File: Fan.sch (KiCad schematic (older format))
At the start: 9 parts, among them Q2 MOSFET_N, Q3 MOSFET_N, Q4 MOSFET_N, U6 MCP4921-E/P, U7 LM324

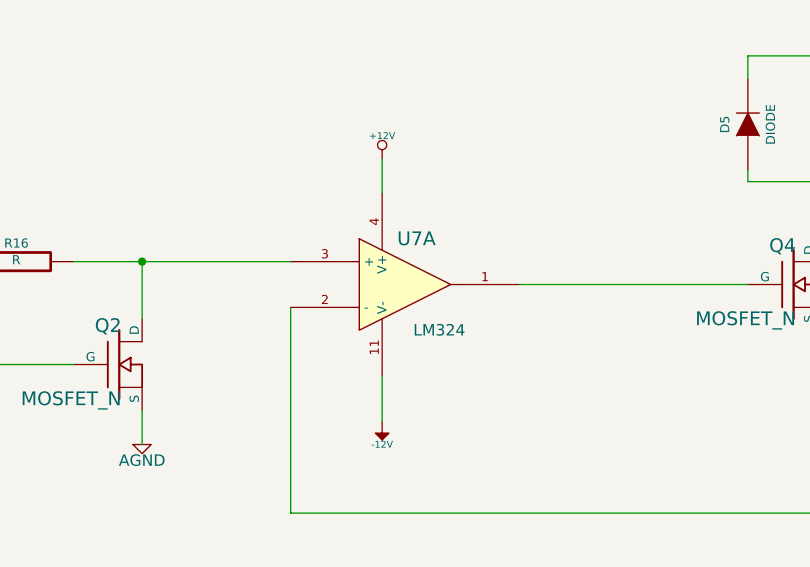
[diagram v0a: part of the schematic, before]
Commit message: Associated Thermocouple module
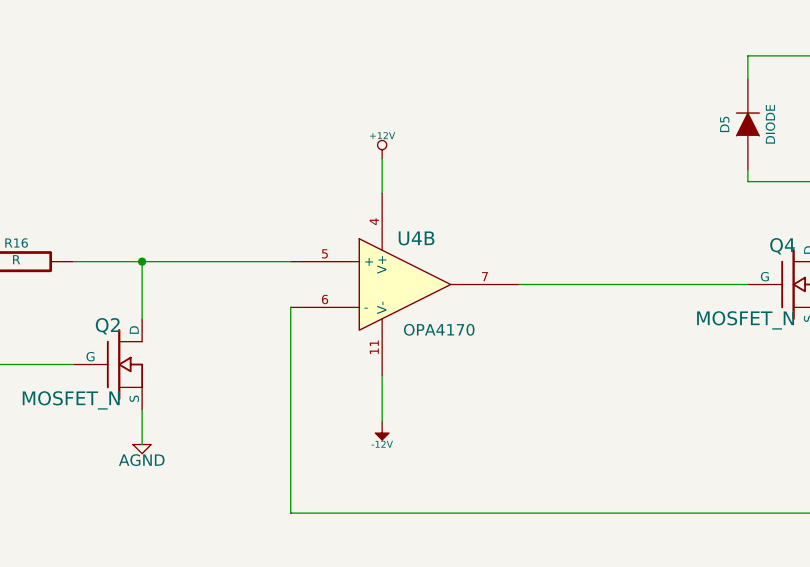
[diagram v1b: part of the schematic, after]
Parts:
- U4: renamed from U7; value LM324 -> OPA4170; MFG Part Number (none) -> OPA4170
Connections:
- net CURR_MEAS: now also U4.6 (-); no longer U4.2 (-)
- net at Q4.G: now also U4.7; no longer U4.1
- net at Q2.D, R16.2: now also U4.5 (+); no longer U4.3 (+)
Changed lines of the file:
@@
 FAN_PWM
 $Comp
-L LM324 U7
-U 1 1 52EF9EF8
+L LM324 U4
+U 2 1 52EF9EF8
 P 4400 2550
-F 0 "U7" H 4450 2750 60  0000 C CNN
-F 1 "LM324" H 4550 2350 50  0000 C CNN
+F 0 "U4" H 4450 2750 60  0000 C CNN
+F 1 "OPA4170" H 4550 2350 50  0000 C CNN
 F 2 "" H 4400 2550 60  0000 C CNN
 F 3 "" H 4400 2550 60  0000 C CNN
-	1    4400 2550
+F 4 "OPA4170" H 4400 2550 60  0001 C CNN "MFG Part Number"
+	2    4400 2550
 	1    0    0    -1
 $EndComp
@@
 $EndComp
 $Comp
-L AGND #PWR34
+L AGND #PWR035
 U 1 1 52EF9F60
 P 6200 4750
-F 0 "#PWR34" H 6200 4750 40  0001 C CNN
+F 0 "#PWR035" H 6200 4750 40  0001 C CNN
 F 1 "AGND" H 6200 4680 50  0000 C CNN
 F 2 "" H 6200 4750 60  0000 C CNN
@@
 	6200 4550 6200 4750
 $Comp
-L +12V #PWR32
+L +12V #PWR036
 U 1 1 52EF9F74
 P 4300 2000
-F 0 "#PWR32" H 4300 1950 20  0001 C CNN
+F 0 "#PWR036" H 4300 1950 20  0001 C CNN
 F 1 "+12V" H 4300 2100 30  0000 C CNN
 F 2 "" H 4300 2000 60  0000 C CNN
@@
 	4300 2000 4300 2150
 $Comp
-L -12V #PWR33
+L -12V #PWR037
 U 1 1 52EF9F84
 P 4300 3150
-F 0 "#PWR33" H 4300 3280 20  0001 C CNN
+F 0 "#PWR037" H 4300 3280 20  0001 C CNN
 F 1 "-12V" H 4300 3250 30  0000 C CNN
 F 2 "" H 4300 3150 60  0000 C CNN
@@
 	850  2500 1300 2500
 $Comp
-L +12V #PWR30
+L +12V #PWR038
 U 1 1 52EFA03F
 P 1750 1900
-F 0 "#PWR30" H 1750 1850 20  0001 C CNN
+F 0 "#PWR038" H 1750 1850 20  0001 C CNN
 F 1 "+12V" H 1750 2000 30  0000 C CNN
 F 2 "" H 1750 1900 60  0000 C CNN
@@
 	2950 2450 3900 2450
 $Comp
-L AGND #PWR31
+L AGND #PWR039
 U 1 1 52EFA16C
 P 3250 3250
-F 0 "#PWR31" H 3250 3250 40  0001 C CNN
+F 0 "#PWR039" H 3250 3250 40  0001 C CNN
 F 1 "AGND" H 3250 3180 50  0000 C CNN
 F 2 "" H 3250 3250 60  0000 C CNN
@@
 FAN_MODE
 $Comp
-L +12C #PWR35
+L +12C #PWR040
 U 1 1 52F168BA
 P 6300 800
-F 0 "#PWR35" H 6300 770 30  0001 C CNN
+F 0 "#PWR040" H 6300 770 30  0001 C CNN
 F 1 "+12C" H 6300 910 40  0000 C CNN
 F 2 "" H 6300 800 60  0000 C CNN

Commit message: more changes?
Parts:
- removed U6: MCP4921-E/P, DIP8, symbol MCP4921-E/P
- added C11, C12: C, symbol C
- added U6: MCP4801, symbol MCP4801
- D5: value DIODE -> B130-13-F; MFG Name (none) -> Diodes Inc; MFG Part Number (none) -> B130-13-F
- Q2: value MOSFET_N -> DMN65D8L-7; MFG Name (none) -> Diodes Inc; MFG Part Number (none) -> DMN65D8L-7
- Q3, Q4: value MOSFET_N -> AOD476; MFG Name (none) -> Alpha and Omega; MFG Part Number (none) -> AOD476
- TH5: value THERMISTOR -> MINISMDC050F-2; MFG Name (none) -> TE Conn; MFG Part Number (none) -> MINISMDC050F-2
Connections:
- net +12C: now also C12.1
- net AGND: now also C11.1, C12.2, U6.7 (Vss)
- net CS_N: now also U6.2 (~CS)
- net MOSI: now also U6.4 (SDI)
- net SCLK: now also U6.3 (SCK)
- net at R16.1: now also U6.8 (Vout)
- new net +5V: C11.2, U6.1 (Vdd)
- new net ~LDAC: U6.5 (~LDAC)
- new net ~SHDN: U6.6 (~SHDN)
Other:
- moved on the sheet: D5, Q2, Q3, Q4, R16, R17, TH5, U4B
